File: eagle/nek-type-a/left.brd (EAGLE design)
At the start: 133 x 116 mm, 69 parts

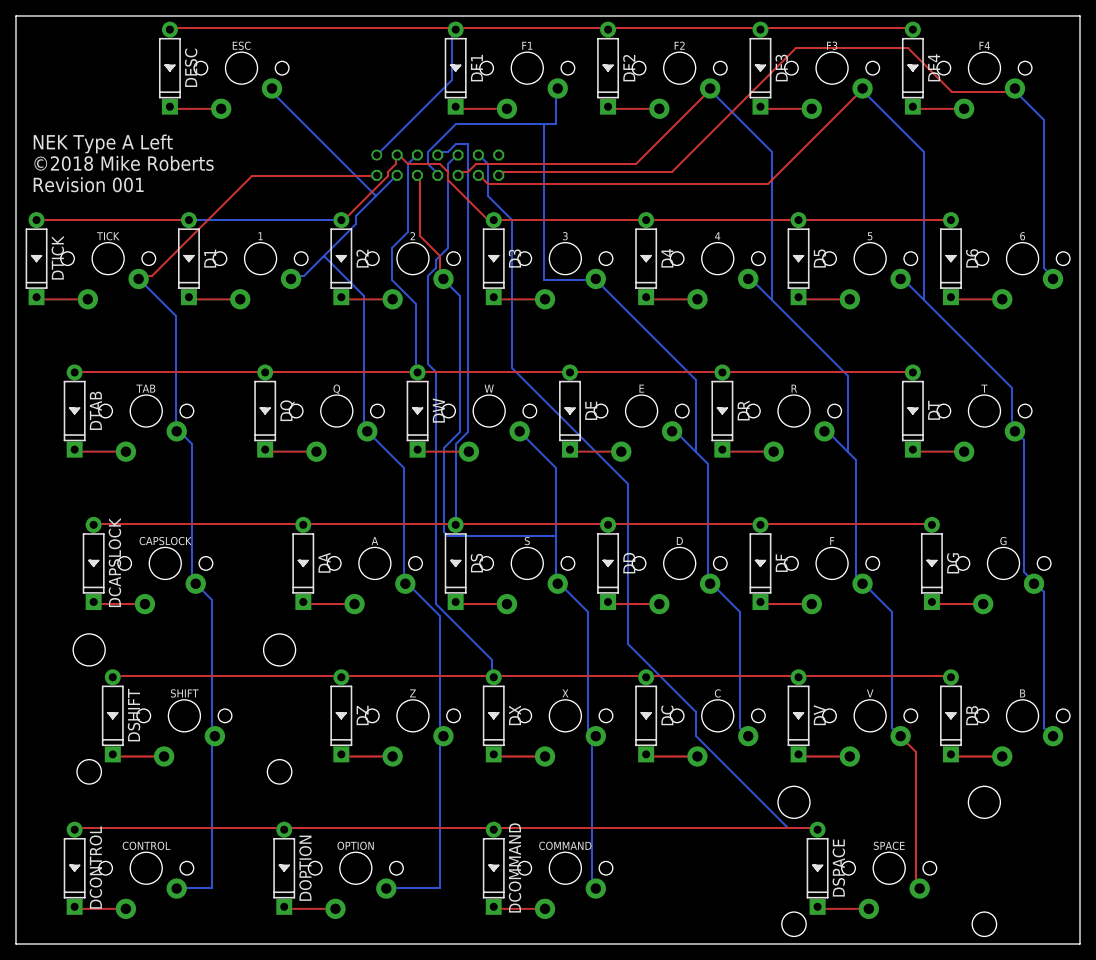
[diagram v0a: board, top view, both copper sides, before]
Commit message: move diodes away from stabilizers
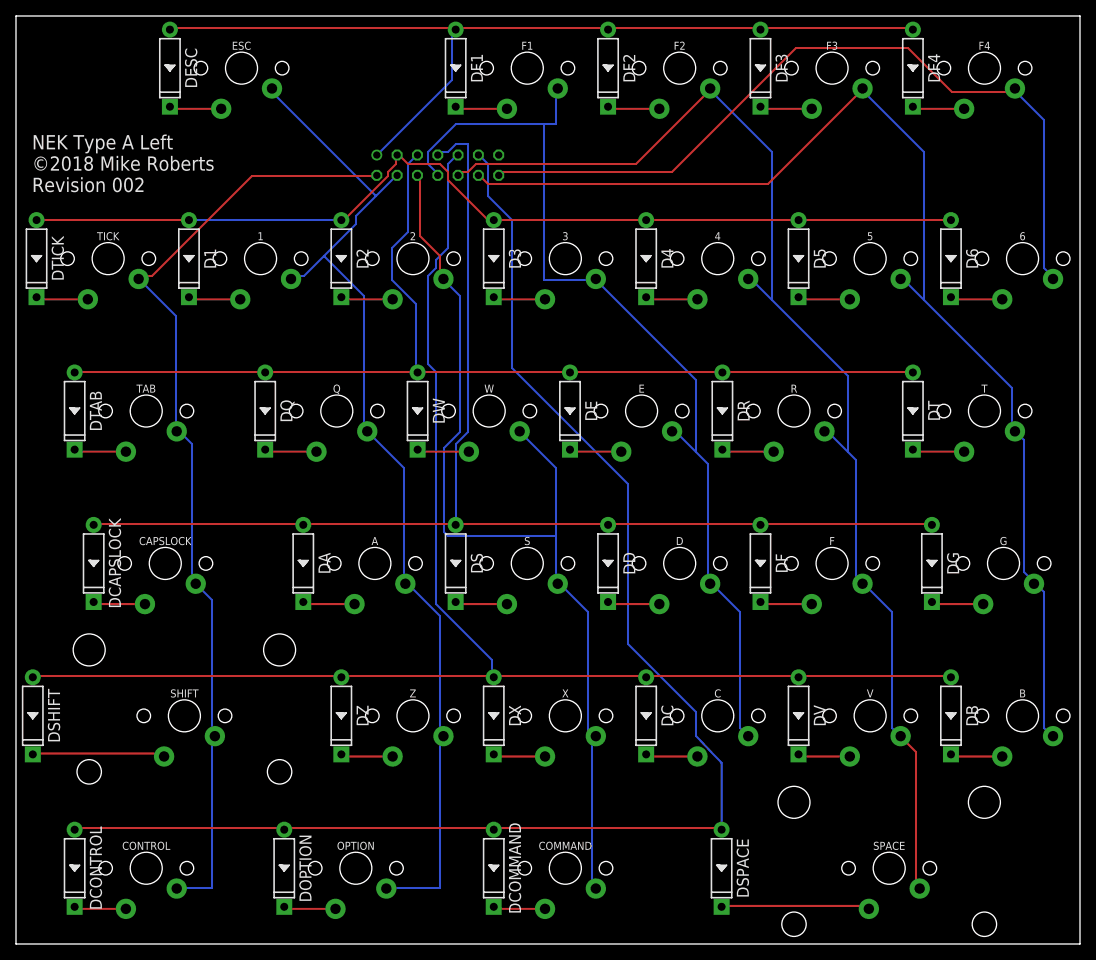
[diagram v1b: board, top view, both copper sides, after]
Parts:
- LEFTCON: value LEFT -> LEFTCON
- moved DSPACE 12.0 mm to (86.2, -109.5)
- moved DSHIFT 10.0 mm to (0.10, -90.5)
- renumbered LEFT to LEFTCON
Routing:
- net ROW6: track 197.4 -> 178.3 mm
- net N$31: track 6.52 -> 18.6 mm
- net N$25: track 6.52 -> 16.6 mm
- net ROW5: track 175.5 -> 185.5 mm
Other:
- board text added: "NEK Type A Left ©2018 Mike Roberts Revision 002"
- board text removed: "NEK Type A Left ©2018 Mike Roberts Revision 001"
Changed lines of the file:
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@@
 <drawing>
 <settings>
-<setting alwaysvectorfont="no"/>
+<setting alwaysvectorfont="yes"/>
 <setting verticaltext="up"/>
 </settings>
@@
 <text x="0" y="-25" size="1.778" layer="25" font="vector" ratio="12">NEK Type A Left
 ©2018 Mike Roberts
-Revision 001</text>
+Revision 002</text>
 <text x="24" y="-25" size="1.778" layer="26" font="vector" ratio="12" rot="MR0">NEK Type A Left
 ©2018 Mike Roberts
-Revision 001</text>
+Revision 002</text>
 </plain>
 <attributes>
@@
 <element name="DR" library="Controller" package="DO-35" value="1N4148" x="86.3" y="-52.38" rot="R270"/>
 <element name="DS" library="Controller" package="DO-35" value="1N4148" x="52.96" y="-71.43" rot="R270"/>
-<element name="DSHIFT" library="Controller" package="DO-35" value="1N4148" x="10.1" y="-90.48" rot="R270"/>
-<element name="DSPACE" library="Controller" package="DO-35" value="1N4148" x="98.2" y="-109.53" rot="R270"/>
+<element name="DSHIFT" library="Controller" package="DO-35" value="1N4148" x="0.1" y="-90.48" rot="R270"/>
+<element name="DSPACE" library="Controller" package="DO-35" value="1N4148" x="86.2" y="-109.53" rot="R270"/>
 <element name="DT" library="Controller" package="DO-35" value="1N4148" x="110.11" y="-52.38" rot="R270"/>
 <element name="DTAB" library="Controller" package="DO-35" value="1N4148" x="5.33" y="-52.38" rot="R270"/>
@@
 <element name="F4" library="Keyboard" package="MX-1U" value="KEYSWITCH-PLAIN-MX-1U" x="119.06" y="-9.52" rot="R180"/>
 <element name="G" library="Keyboard" package="MX-1U" value="KEYSWITCH-PLAIN-MX-1U" x="121.44" y="-71.43" rot="R180"/>
-<element name="LEFT" library="con-harting" library_urn="urn:adsk.eagle:library:151" package="CON14" package3d_urn="urn:adsk.eagle:package:7117/1" value="LEFT" x="50.72" y="-21.65" rot="MR180">
+<element name="LEFTCON" library="con-harting" library_urn="urn:adsk.eagle:library:151" package="CON14" package3d_urn="urn:adsk.eagle:package:7117/1" value="LEFTCON" x="50.72" y="-21.65" rot="MR180">
 <attribute name="MF" value="" x="50.72" y="-21.65" size="1.778" layer="28" rot="MR180" display="off"/>
 <attribute name="MPN" value="" x="50.72" y="-21.65" size="1.778" layer="28" rot="MR180" display="off"/>
@@
 <contactref element="DF3" pad="C"/>
 <contactref element="DF4" pad="C"/>
-<contactref element="LEFT" pad="1"/>
+<contactref element="LEFTCON" pad="1"/>
 <wire x1="91" y1="-4.5" x2="72.5" y2="-4.5" width="0.254" layer="1"/>
 <wire x1="72.5" y1="-4.5" x2="72.01" y2="-4.7" width="0.254" layer="1"/>
@@
 <contactref element="D5" pad="C"/>
 <contactref element="D6" pad="C"/>
-<contactref element="LEFT" pad="3"/>
+<contactref element="LEFTCON" pad="3"/>
 <wire x1="45.5" y1="-21.5" x2="45.5" y2="-20.5" width="0.254" layer="1"/>
 <wire x1="44.5" y1="-22.5" x2="45.5" y2="-21.5" width="0.254" layer="1"/>
@@
 <contactref element="DR" pad="C"/>
 <contactref element="DT" pad="C"/>
-<contactref element="LEFT" pad="5"/>
+<contactref element="LEFTCON" pad="5"/>
 <wire x1="86" y1="-47.5" x2="67.5" y2="-47.5" width="0.254" layer="1"/>
 <wire x1="67.5" y1="-47.5" x2="67.25" y2="-47.56" width="0.254" layer="1"/>
@@
 <contactref element="DF" pad="C"/>
 <contactref element="DG" pad="C"/>
-<contactref element="LEFT" pad="7"/>
+<contactref element="LEFTCON" pad="7"/>
 <wire x1="91" y1="-66.5" x2="72.5" y2="-66.5" width="0.254" layer="1"/>
 <wire x1="72.5" y1="-66.5" x2="72.01" y2="-66.61" width="0.254" layer="1"/>
@@
 <contactref element="DV" pad="C"/>
 <contactref element="DB" pad="C"/>
-<contactref element="LEFT" pad="9"/>
+<contactref element="LEFTCON" pad="9"/>
 <wire x1="95.5" y1="-85.5" x2="77" y2="-85.5" width="0.254" layer="1"/>
 <wire x1="77" y1="-85.5" x2="76.77" y2="-85.66" width="0.254" layer="1"/>
@@
 <wire x1="114.5" y1="-85.5" x2="114.87" y2="-85.66" width="0.254" layer="1"/>
 <wire x1="96" y1="-85.5" x2="95.82" y2="-85.66" width="0.254" layer="1"/>
-<wire x1="38.5" y1="-85.5" x2="10.5" y2="-85.5" width="0.254" layer="1"/>
-<wire x1="10.5" y1="-85.5" x2="10.1" y2="-85.66" width="0.254" layer="1"/>
+<wire x1="38.5" y1="-85.5" x2="0.5" y2="-85.5" width="0.254" layer="1"/>
+<wire x1="0.5" y1="-85.5" x2="0.1" y2="-85.66" width="0.254" layer="1"/>
 <wire x1="38.5" y1="-85.5" x2="38.67" y2="-85.66" width="0.254" layer="1"/>
 <wire x1="52" y1="-21.5" x2="53" y2="-20.5" width="0.254" layer="16"/>
@@
 <contactref element="DCOMMAND" pad="C"/>
 <contactref element="DSPACE" pad="C"/>
-<contactref element="LEFT" pad="11"/>
+<contactref element="LEFTCON" pad="11"/>
 <wire x1="31.5" y1="-104.5" x2="5.5" y2="-104.5" width="0.254" layer="1"/>
 <wire x1="5.5" y1="-104.5" x2="5.33" y2="-104.71" width="0.254" layer="1"/>
@@
 <wire x1="83" y1="-90" x2="74.5" y2="-81.5" width="0.254" layer="16"/>
 <wire x1="83" y1="-93" x2="83" y2="-90" width="0.254" layer="16"/>
-<wire x1="94.5" y1="-104.5" x2="83" y2="-93" width="0.254" layer="16"/>
-<wire x1="98" y1="-104.5" x2="94.5" y2="-104.5" width="0.254" layer="16"/>
 <wire x1="56" y1="-20.5" x2="55.8" y2="-20.38" width="0.254" layer="16"/>
-<wire x1="98" y1="-104.5" x2="98.2" y2="-104.71" width="0.254" layer="16"/>
-<wire x1="98" y1="-104.5" x2="58" y2="-104.5" width="0.254" layer="1"/>
+<wire x1="83" y1="-93" x2="86.2" y2="-96.36" width="0.254" layer="16"/>
+<wire x1="86" y1="-104.5" x2="58" y2="-104.5" width="0.254" layer="1"/>
 <wire x1="58" y1="-104.5" x2="57.72" y2="-104.71" width="0.254" layer="1"/>
-<wire x1="98" y1="-104.5" x2="98.2" y2="-104.71" width="0.254" layer="1"/>
+<wire x1="86" y1="-104.5" x2="86.2" y2="-104.71" width="0.254" layer="1"/>
+<wire x1="86.2" y1="-96.36" x2="86.2" y2="-104.71" width="0.254" layer="16"/>
 </signal>
 <signal name="N$1">
@@
 <contactref element="SHIFT" pad="MX2"/>
 <contactref element="DSHIFT" pad="A"/>
-<wire x1="10.1" y1="-95.3" x2="10.36" y2="-95.56" width="0.254" layer="1"/>
-<wire x1="10.36" y1="-95.56" x2="16.51" y2="-95.56" width="0.254" layer="1"/>
+<wire x1="0.1" y1="-95.3" x2="0.207015625" y2="-95.192984375" width="0.254" layer="1"/>
+<wire x1="0.207015625" y1="-95.192984375" x2="16.142984375" y2="-95.192984375" width="0.254" layer="1"/>
+<wire x1="16.142984375" y1="-95.192984375" x2="16.51" y2="-95.56" width="0.254" layer="1"/>
 </signal>
 <signal name="N$26">
@@
 <contactref element="SPACE" pad="MX2"/>
 <contactref element="DSPACE" pad="A"/>
-<wire x1="98.2" y1="-114.35" x2="98.46" y2="-114.61" width="0.254" layer="1"/>
-<wire x1="98.46" y1="-114.61" x2="104.61" y2="-114.61" width="0.254" layer="1"/>
+<wire x1="86.2" y1="-114.35" x2="86.307015625" y2="-114.242984375" width="0.254" layer="1"/>
+<wire x1="86.307015625" y1="-114.242984375" x2="104.242984375" y2="-114.242984375" width="0.254" layer="1"/>
+<wire x1="104.242984375" y1="-114.242984375" x2="104.61" y2="-114.61" width="0.254" layer="1"/>
 </signal>
 <signal name="N$32">
@@
 <contactref element="SHIFT" pad="MX1"/>
 <contactref element="CONTROL" pad="MX1"/>
-<contactref element="LEFT" pad="2"/>
+<contactref element="LEFTCON" pad="2"/>
 <wire x1="27.5" y1="-23" x2="43" y2="-23" width="0.254" layer="1"/>
 <wire x1="15" y1="-35.5" x2="27.5" y2="-23" width="0.254" layer="1"/>
@@
 <contactref element="T" pad="MX1"/>
 <contactref element="5" pad="MX1"/>
-<contactref element="LEFT" pad="12"/>
+<contactref element="LEFTCON" pad="12"/>
 <contactref element="F3" pad="MX1"/>
 <wire x1="57" y1="-24" x2="56" y2="-23" width="0.254" layer="1"/>
@@
 </signal>
 <signal name="COL3">
-<contactref element="LEFT" pad="6"/>
+<contactref element="LEFTCON" pad="6"/>
 <contactref element="COMMAND" pad="MX1"/>
 <contactref element="X" pad="MX1"/>
@@
 </signal>
 <signal name="COL7">
-<contactref element="LEFT" pad="14"/>
+<contactref element="LEFTCON" pad="14"/>
 <contactref element="F4" pad="MX1"/>
 <contactref element="6" pad="MX1"/>
@@
 </signal>
 <signal name="COL2">
-<contactref element="LEFT" pad="4"/>
+<contactref element="LEFTCON" pad="4"/>
 <contactref element="OPTION" pad="MX1"/>
 <contactref element="Z" pad="MX1"/>
@@
 </signal>
 <signal name="COL5">
-<contactref element="LEFT" pad="10"/>
+<contactref element="LEFTCON" pad="10"/>
 <contactref element="F2" pad="MX1"/>
 <contactref element="SPACE" pad="MX1"/>
@@
 </signal>
 <signal name="COL4">
-<contactref element="LEFT" pad="8"/>
+<contactref element="LEFTCON" pad="8"/>
 <contactref element="F1" pad="MX1"/>
 <contactref element="C" pad="MX1"/>
